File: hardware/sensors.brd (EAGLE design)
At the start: 80 x 80 mm, 30 parts, among them U1 DS18B20, U2 DS18B20, U3 DS18B20

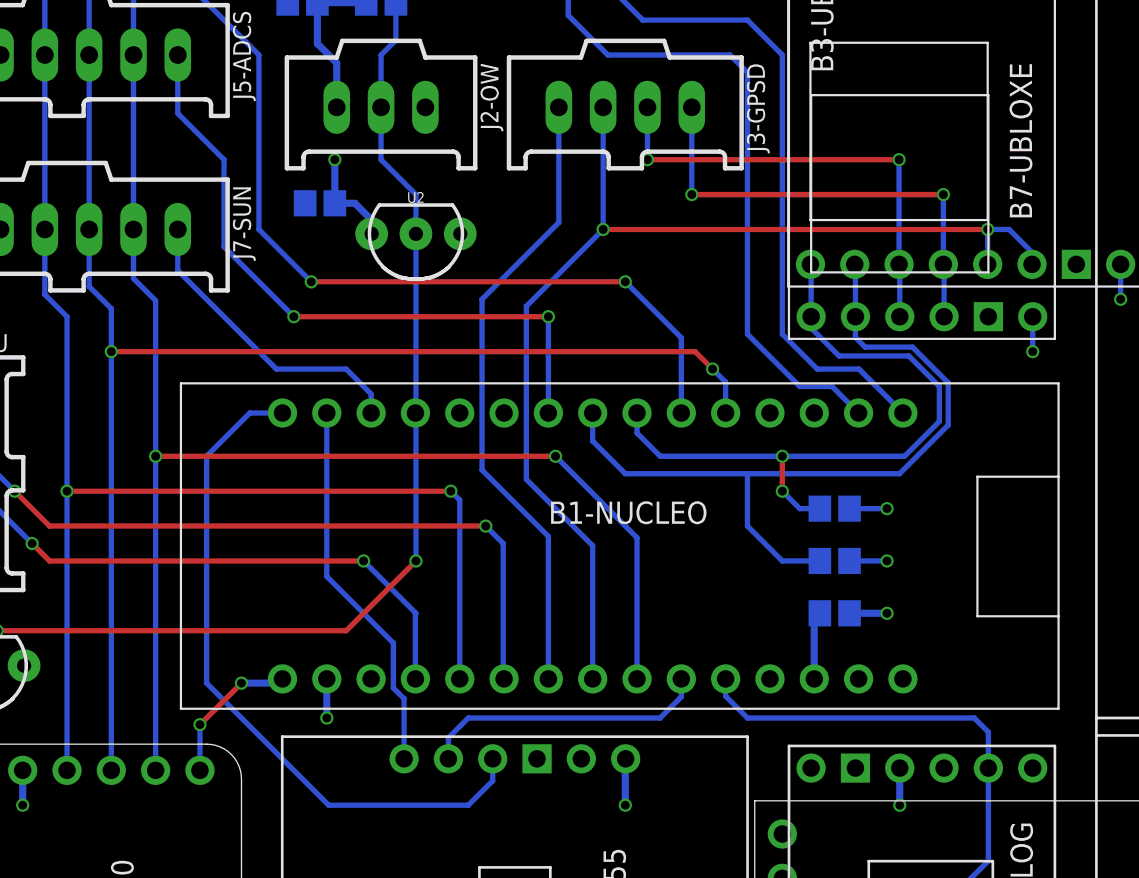
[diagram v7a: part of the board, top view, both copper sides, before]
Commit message: Add I2C connector
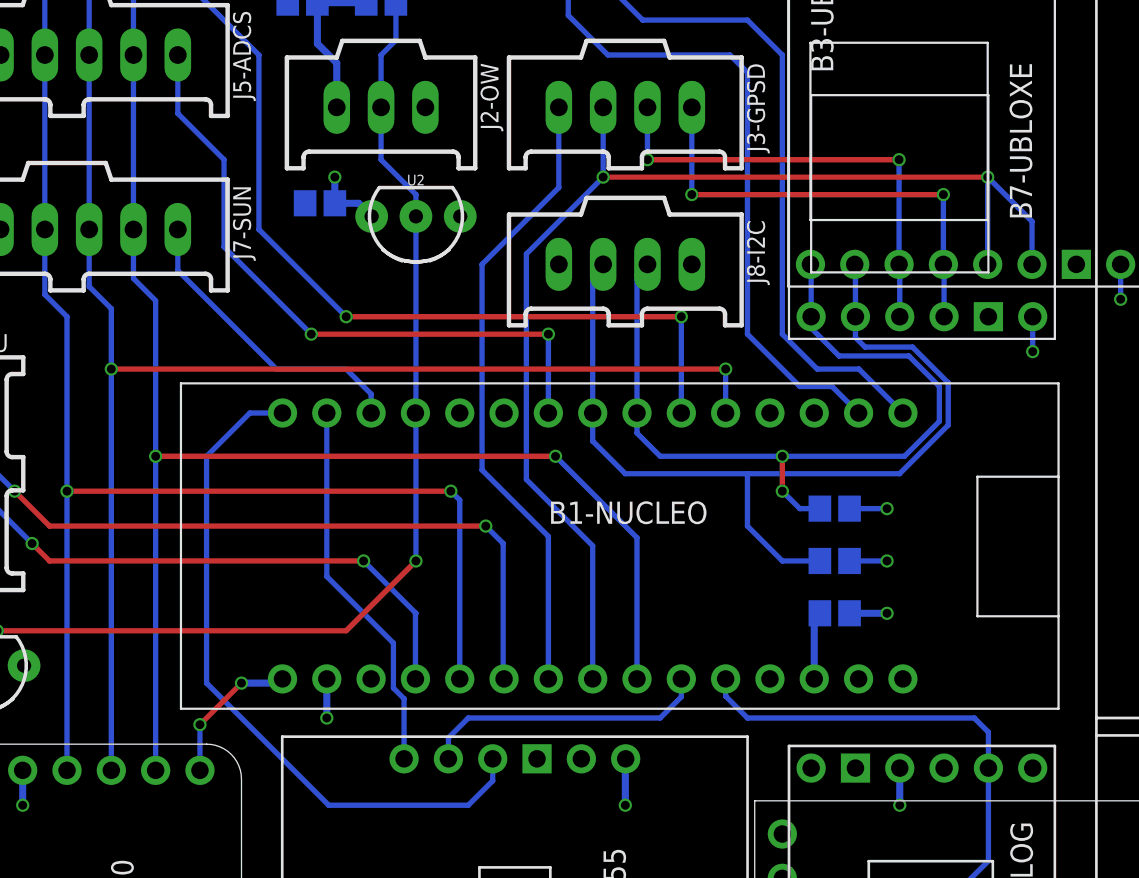
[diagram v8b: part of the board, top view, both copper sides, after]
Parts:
- added J8-I2C: (no value), con-molex-c-grid:90136-1?04
- moved U2 1.00 mm to (36.0, 55.8)
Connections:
- net GND: now also J8-I2C.1
- net GPS-SCL: now also J8-I2C.3
- net GPS-SDA: now also J8-I2C.2
- net VCC: now also J8-I2C.4
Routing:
- net GPS-SDA: track 38.8 -> 47.6 mm
- net GPS-SCL: track 44.9 -> 53.7 mm
- net GPS-TP: track 64.0 -> 69.3 mm
- net VCC: track 88.9 -> 87.0 mm
- net SPI-CS-ENV0: track 53.0 -> 53.7 mm
- net SPI-CS-ADCS: track 37.9 -> 37.3 mm
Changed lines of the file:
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@@
 <wire x1="11.7" y1="38.1" x2="11.7" y2="36.2" width="0.1016" layer="41"/>
 <wire x1="11.7" y1="36.2" x2="8.3" y2="36.2" width="0.1016" layer="41"/>
-<circle x="33.45" y="54.75" radius="1.097721875" width="0.1016" layer="41"/>
+<circle x="33.45" y="55.75" radius="1.097721875" width="0.1016" layer="41"/>
 <circle x="30.45" y="74" radius="1.097721875" width="0.1016" layer="41"/>
 <circle x="8.45" y="30" radius="1.097721875" width="0.1016" layer="41"/>
@@
 <attribute name="STORE_ID" value="SEN-00245" x="11" y="30" size="1.778" layer="27" rot="R180" display="off"/>
 </element>
-<element name="U2" library="Frcy" package="TO-92-AMMO" value="DS18B20" x="36" y="54.75" rot="R180">
-<attribute name="STORE_ID" value="SEN-00245" x="36" y="54.75" size="1.778" layer="27" rot="R180" display="off"/>
+<element name="U2" library="Frcy" package="TO-92-AMMO" value="DS18B20" x="36" y="55.75" rot="R180">
+<attribute name="STORE_ID" value="SEN-00245" x="36" y="55.75" size="1.778" layer="27" rot="R180" display="off"/>
 </element>
 <element name="R2" library="rcl" library_urn="urn:adsk.eagle:library:334" package="R2012" package3d_urn="urn:adsk.eagle:package:23543/2" value="10k" x="60" y="33" rot="MR0">
@@
 <element name="B6-BLE" library="Frcy" package="HUAMAO-HM-11" value="" x="57" y="14" rot="R270"/>
 <element name="B7-UBLOXE" library="Frcy" package="UPUTRONICS-UBLOX-M8Q" value="" x="67.5" y="53"/>
+<element name="J8-I2C" library="con-molex-c-grid" package="90136-1?04" value="" x="48" y="53" rot="R180"/>
 </elements>
 <signals>
@@
 <contactref element="R1" pad="2"/>
 <wire x1="30.35" y1="68" x2="33.15" y2="68" width="0.4064" layer="16"/>
-<wire x1="33.46" y1="54.75" x2="33.46" y2="55.54" width="0.4064" layer="16"/>
-<wire x1="32.5" y1="56.5" x2="31.35" y2="56.5" width="0.4064" layer="16"/>
-<wire x1="33.46" y1="55.54" x2="32.5" y2="56.5" width="0.4064" layer="16"/>
-<via x="31.35" y="59" extent="1-16" drill="0.508"/>
-<wire x1="31.35" y1="56.5" x2="31.35" y2="59" width="0.4064" layer="16"/>
+<via x="31.35" y="58" extent="1-16" drill="0.508"/>
 <wire x1="30.46" y1="74" x2="27.85" y2="74" width="0.4064" layer="16"/>
 <wire x1="27.85" y1="74" x2="28" y2="73.85" width="0.4064" layer="16"/>
@@
 <wire x1="71.35" y1="50" x2="71.35" y2="48" width="0.3048" layer="16"/>
 <via x="71.35" y="48" extent="1-16" drill="0.508"/>
+<contactref element="J8-I2C" pad="4"/>
+<wire x1="33.46" y1="55.75" x2="32.71" y2="56.5" width="0.4064" layer="16"/>
+<wire x1="32.71" y1="56.5" x2="31.35" y2="56.5" width="0.4064" layer="16"/>
+<wire x1="31.35" y1="56.5" x2="31.35" y2="58" width="0.4064" layer="16"/>
 </signal>
 <signal name="GND">
@@
 <contactref element="B6-BLE" pad="GND"/>
 <contactref element="B7-UBLOXE" pad="GND"/>
+<contactref element="J8-I2C" pad="1"/>
 </signal>
 <signal name="IMU-SDA">
@@
 <wire x1="58.65" y1="50" x2="58.65" y2="52.96" width="0.3048" layer="16"/>
 <wire x1="58.65" y1="52.96" x2="58.61" y2="53" width="0.3048" layer="16"/>
+<contactref element="J8-I2C" pad="2"/>
+<wire x1="48.67" y1="44.48" x2="48.67" y2="52.4" width="0.3048" layer="16"/>
+<wire x1="48.67" y1="52.4" x2="49.27" y2="53" width="0.3048" layer="16"/>
 </signal>
 <signal name="GPS-SCL">
@@
 <wire x1="55" y1="38" x2="55" y2="41" width="0.3048" layer="16"/>
 <wire x1="57" y1="36" x2="55" y2="38" width="0.3048" layer="16"/>
+<contactref element="J8-I2C" pad="3"/>
+<wire x1="46.13" y1="44.48" x2="46.13" y2="52.4" width="0.3048" layer="16"/>
+<wire x1="46.13" y1="52.4" x2="46.73" y2="53" width="0.3048" layer="16"/>
 </signal>
 <signal name="LOG-TX">
@@
 <wire x1="17.27" y1="75" x2="17.27" y2="65" width="0.3048" layer="16"/>
 <wire x1="17.27" y1="65" x2="17.27" y2="55" width="0.3048" layer="16"/>
-<wire x1="53.75" y1="44.48" x2="53.75" y2="46.25" width="0.3048" layer="16"/>
-<wire x1="53.75" y1="46.25" x2="53" y2="47" width="0.3048" layer="16"/>
-<via x="53" y="47" extent="1-16" drill="0.508"/>
-<wire x1="53" y1="47" x2="52" y2="48" width="0.3048" layer="1"/>
-<wire x1="18.54" y1="24" x2="18.54" y2="48" width="0.3048" layer="16"/>
-<wire x1="18.54" y1="48" x2="18.54" y2="50.46" width="0.3048" layer="16"/>
+<wire x1="18.54" y1="24" x2="18.54" y2="47" width="0.3048" layer="16"/>
+<wire x1="18.54" y1="47" x2="18.54" y2="50.46" width="0.3048" layer="16"/>
 <wire x1="17.27" y1="51.73" x2="17.27" y2="55" width="0.3048" layer="16"/>
 <wire x1="18.54" y1="50.46" x2="17.27" y2="51.73" width="0.3048" layer="16"/>
-<wire x1="52" y1="48" x2="18.54" y2="48" width="0.3048" layer="1"/>
-<via x="18.54" y="48" extent="1-16" drill="0.508"/>
+<via x="18.54" y="47" extent="1-16" drill="0.508"/>
+<wire x1="53.75" y1="44.48" x2="53.75" y2="47" width="0.3048" layer="16"/>
+<via x="53.75" y="47" extent="1-16" drill="0.508"/>
+<wire x1="18.54" y1="47" x2="53.75" y2="47" width="0.3048" layer="1"/>
 </signal>
 <signal name="SPI-CS-ADCS">
 <contactref element="B1-NUCLEO" pad="D6"/>
 <contactref element="J5-ADCS" pad="1"/>
-<via x="29" y="50" extent="1-16" drill="0.508"/>
-<wire x1="29" y1="50" x2="25" y2="54" width="0.3048" layer="16"/>
+<via x="30" y="49" extent="1-16" drill="0.508"/>
+<wire x1="30" y1="49" x2="25" y2="54" width="0.3048" layer="16"/>
 <wire x1="25" y1="54" x2="25" y2="59" width="0.3048" layer="16"/>
 <wire x1="22.35" y1="61.65" x2="22.35" y2="65" width="0.3048" layer="16"/>
 <wire x1="25" y1="59" x2="22.35" y2="61.65" width="0.3048" layer="16"/>
-<wire x1="29" y1="50" x2="43.59" y2="50" width="0.3048" layer="1"/>
-<wire x1="43.59" y1="44.48" x2="43.59" y2="50" width="0.3048" layer="16"/>
-<via x="43.59" y="50" extent="1-16" drill="0.508"/>
+<wire x1="30" y1="49" x2="43.59" y2="49" width="0.3048" layer="1"/>
+<wire x1="43.59" y1="44.48" x2="43.59" y2="49" width="0.3048" layer="16"/>
+<via x="43.59" y="49" extent="1-16" drill="0.508"/>
 </signal>
 <signal name="TEMP-OW">
@@
 <wire x1="34.85" y1="65.85" x2="34" y2="65" width="0.3048" layer="16"/>
 <wire x1="35.97" y1="44.48" x2="36" y2="44.51" width="0.3048" layer="16"/>
-<wire x1="36" y1="44.51" x2="36" y2="54.75" width="0.3048" layer="16"/>
-<wire x1="36" y1="54.75" x2="36" y2="57" width="0.3048" layer="16"/>
-<wire x1="36" y1="57" x2="34" y2="59" width="0.3048" layer="16"/>
+<wire x1="36" y1="44.51" x2="36" y2="55.75" width="0.3048" layer="16"/>
 <wire x1="34" y1="59" x2="34" y2="62" width="0.3048" layer="16"/>
 <wire x1="34.85" y1="68" x2="34.85" y2="70.15" width="0.3048" layer="16"/>
@@
 <wire x1="12" y1="32" x2="11" y2="31" width="0.4064" layer="16"/>
 <wire x1="11" y1="31" x2="11" y2="30" width="0.4064" layer="16"/>
+<wire x1="36" y1="55.75" x2="36" y2="57" width="0.3048" layer="16"/>
+<wire x1="36" y1="57" x2="34" y2="59" width="0.3048" layer="16"/>
 </signal>
 <signal name="SPI-SCK">
@@
 <contactref element="B1-NUCLEO" pad="D3"/>
 <contactref element="J6-ENV" pad="1"/>
-<via x="30" y="52" extent="1-16" drill="0.508"/>
-<wire x1="30" y1="52" x2="27" y2="55" width="0.3048" layer="16"/>
+<via x="32" y="50" extent="1-16" drill="0.508"/>
+<wire x1="32" y1="50" x2="27" y2="55" width="0.3048" layer="16"/>
 <wire x1="27" y1="55" x2="27" y2="65" width="0.3048" layer="16"/>
-<via x="48" y="52" extent="1-16" drill="0.508"/>
-<wire x1="30" y1="52" x2="48" y2="52" width="0.3048" layer="1"/>
-<wire x1="48" y1="52" x2="51.21" y2="48.79" width="0.3048" layer="16"/>
-<wire x1="51.21" y1="48.79" x2="51.21" y2="44.48" width="0.3048" layer="16"/>
 <wire x1="22.35" y1="69.65" x2="22.35" y2="75" width="0.3048" layer="16"/>
 <wire x1="27" y1="65" x2="22.35" y2="69.65" width="0.3048" layer="16"/>
+<wire x1="51.21" y1="44.48" x2="51.21" y2="50" width="0.3048" layer="16"/>
+<via x="51.21" y="50" extent="1-16" drill="0.508"/>
+<wire x1="32" y1="50" x2="51.21" y2="50" width="0.3048" layer="1"/>
 </signal>
 <signal name="DBG-TX">
@@
 <wire x1="43.59" y1="29.24" x2="43.59" y2="37.41" width="0.3048" layer="16"/>
 <wire x1="43.59" y1="37.41" x2="39.788" y2="41.212" width="0.3048" layer="16"/>
-<wire x1="39.788" y1="41.212" x2="39.788" y2="51" width="0.3048" layer="16"/>
-<wire x1="39.788" y1="51" x2="44.19" y2="55.402" width="0.3048" layer="16"/>
-<wire x1="44.19" y1="55.402" x2="44.19" y2="62" width="0.3048" layer="16"/>
+<wire x1="39.788" y1="41.212" x2="39.788" y2="53" width="0.3048" layer="16"/>
+<wire x1="39.788" y1="53" x2="44.19" y2="57.402" width="0.3048" layer="16"/>
+<wire x1="44.19" y1="57.402" x2="44.19" y2="62" width="0.3048" layer="16"/>
 </signal>
 <signal name="VIN">
@@
 <wire x1="46.13" y1="29.24" x2="46.13" y2="36.87" width="0.3048" layer="16"/>
 <wire x1="46.13" y1="36.87" x2="42.328" y2="40.672" width="0.3048" layer="16"/>
-<wire x1="42.328" y1="40.672" x2="42.328" y2="50.598" width="0.3048" layer="16"/>
-<wire x1="68.77" y1="53" x2="68.77" y2="55" width="0.3048" layer="16"/>
-<wire x1="46.73" y1="62" x2="46.73" y2="55" width="0.3048" layer="16"/>
-<via x="68.77" y="55" extent="1-16" drill="0.508"/>
-<wire x1="68.77" y1="55" x2="46.73" y2="55" width="0.3048" layer="1"/>
-<via x="46.73" y="55" extent="1-16" drill="0.508"/>
-<wire x1="46.73" y1="55" x2="42.328" y2="50.598" width="0.3048" layer="16"/>
-<wire x1="68.77" y1="55" x2="70" y2="55" width="0.3048" layer="16"/>
-<wire x1="70" y1="55" x2="71.31" y2="53.69" width="0.3048" layer="16"/>
-<wire x1="71.31" y1="53.69" x2="71.31" y2="53" width="0.3048" layer="16"/>
+<wire x1="42.328" y1="40.672" x2="42.328" y2="53.598" width="0.3048" layer="16"/>
+<wire x1="68.77" y1="53" x2="68.77" y2="58" width="0.3048" layer="16"/>
+<wire x1="46.73" y1="62" x2="46.73" y2="58" width="0.3048" layer="16"/>
+<via x="68.77" y="58" extent="1-16" drill="0.508"/>
+<wire x1="68.77" y1="58" x2="46.73" y2="58" width="0.3048" layer="1"/>
+<via x="46.73" y="58" extent="1-16" drill="0.508"/>
+<wire x1="46.73" y1="58" x2="42.328" y2="53.598" width="0.3048" layer="16"/>
+<wire x1="71.31" y1="53" x2="71.31" y2="55.46" width="0.3048" layer="16"/>
+<wire x1="71.31" y1="55.46" x2="68.77" y2="58" width="0.3048" layer="16"/>
 </signal>
 </signals>
